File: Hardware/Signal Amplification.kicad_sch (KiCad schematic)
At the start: 0 parts

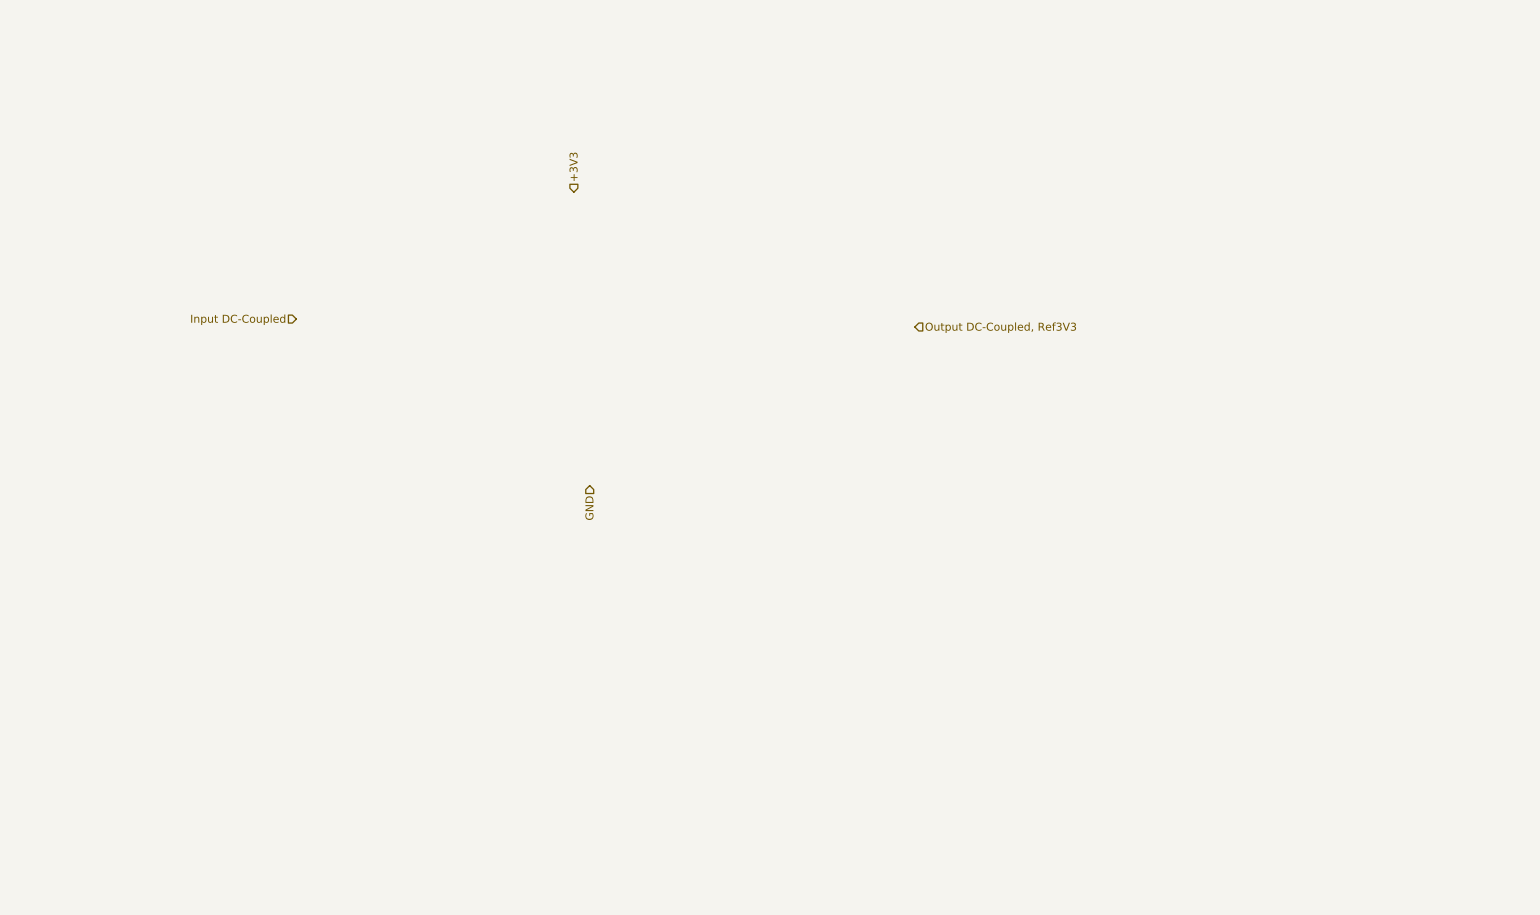
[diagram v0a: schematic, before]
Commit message: Drew the analog Signal conditioning
The analog signal conditioning can be reduced to:
- a amplification by -60
- a High-Pass filter with Fc≈20Hz -3dB
- a Low-Pass filter with Fc≈5kHz -6dB
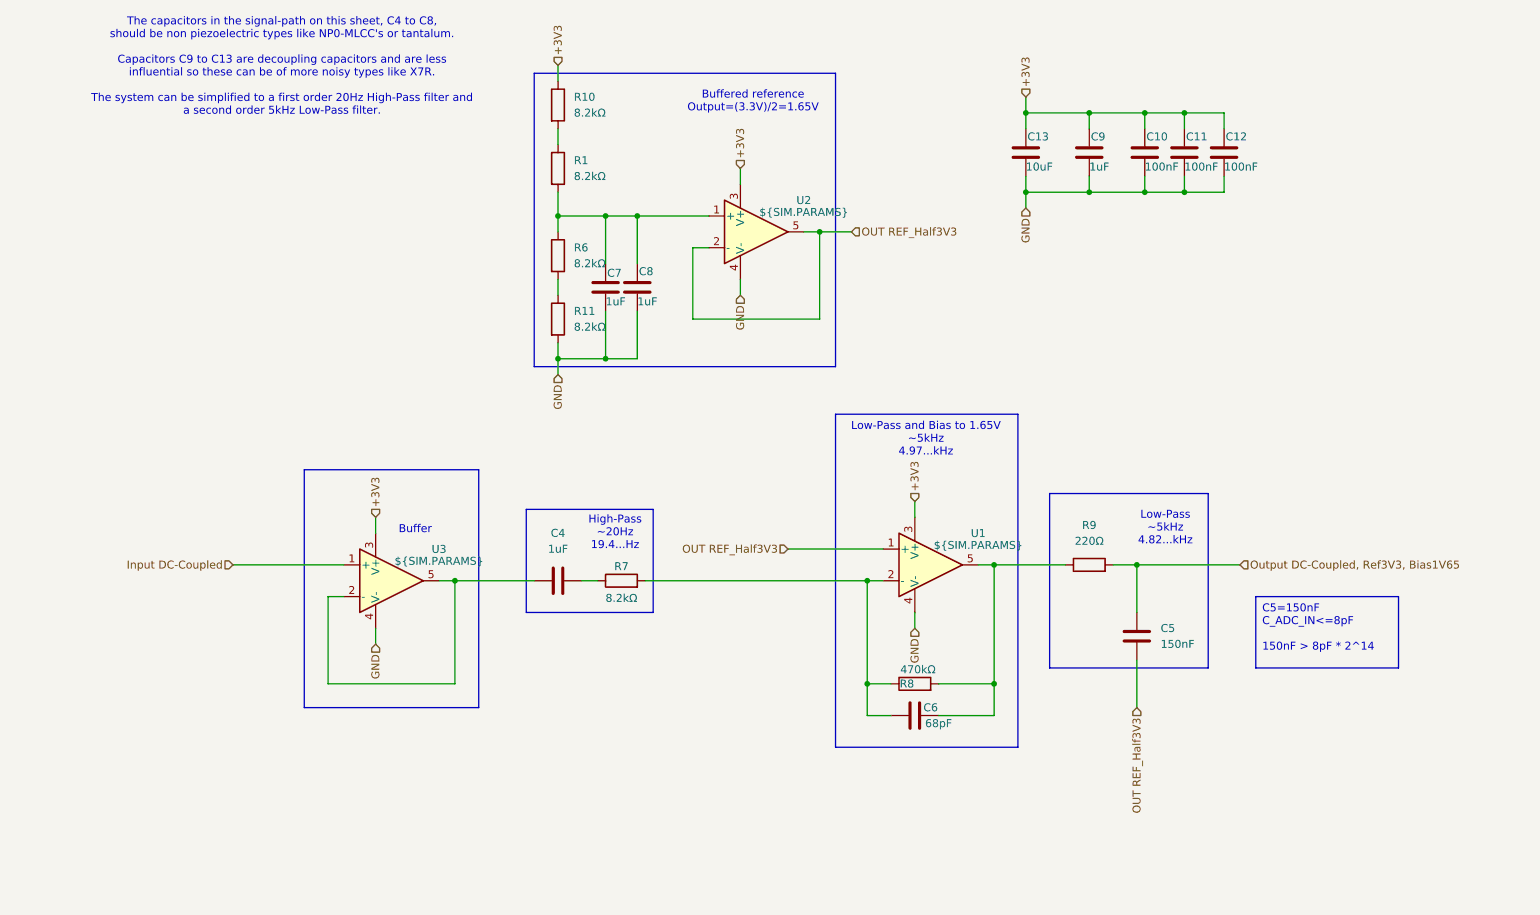
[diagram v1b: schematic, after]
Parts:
- added C10, C11, C12: 100nF, symbol Device:C
- added C13: 10uF, symbol Device:C
- added C4, C7, C8, C9: 1uF, symbol Device:C
- added C5: 150nF, symbol Device:C
- added C6: 68pF, symbol Device:C
- added R1, R10, R11, R6, R7: 8.2kΩ, symbol Device:R
- added R8: 470kΩ, symbol Device:R
- added R9: 220Ω, symbol Device:R
- added U1, U2, U3: ${SIM.PARAMS}, symbol Simulation_SPICE:OPAMP
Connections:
- net +3V3: now also C10.1, C11.1, C12.1, C13.1, C9.1, R10.1, U1.3 (V+), U2.3 (V+), U3.3 (V+)
- net GND: now also C10.2, C11.2, C12.2, C13.2, C7.2, C8.2, C9.2, R11.2, U1.4 (V-), U2.4 (V-), U3.4 (V-)
- net Input DC-Coupled: now also U3.1 (+)
- new net: C7.1, C8.1, R1.2, R6.1, U2.1 (+)
- new net: R11.1, R6.2
- new net: C6.2, R8.2, R9.1, U1.5
- new net: C4.2, R7.1
- new net: C6.1, R7.2, R8.1, U1.2 (-)
- new net: C4.1, U3.2 (-), U3.5
- new net: R1.1, R10.2
- new net OUT REF_Half3V3: C5.2, U1.1 (+), U2.2 (-), U2.5
- new net Output DC-Coupled, Ref3V3, Bias1V65: C5.1, R9.2
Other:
- note added: "Buffer"
- note added: "Buffered reference Output=(3.3V)/2=1.65V"
- note added: "High-Pass ~20Hz 19.4...Hz"
- note added: "Low-Pass and Bias to 1.65V ~5kHz 4.97...kHz"
- note added: "Low-Pass ~5kHz 4.82...kHz"
- note added: "The capacitors in the signal-path on this sheet, C4 to C8, should be non piezoelectric types like NP0-MLCC's or tantalum. Capacitors C9 to C13 are decoupling capacitors and are less influential so these can be of more noisy types like X7R. The system can be simplified to a first order 20Hz High-Pass filter and a second order 5kHz Low-Pass filter."

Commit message: split some of the text and grouped the circuits better
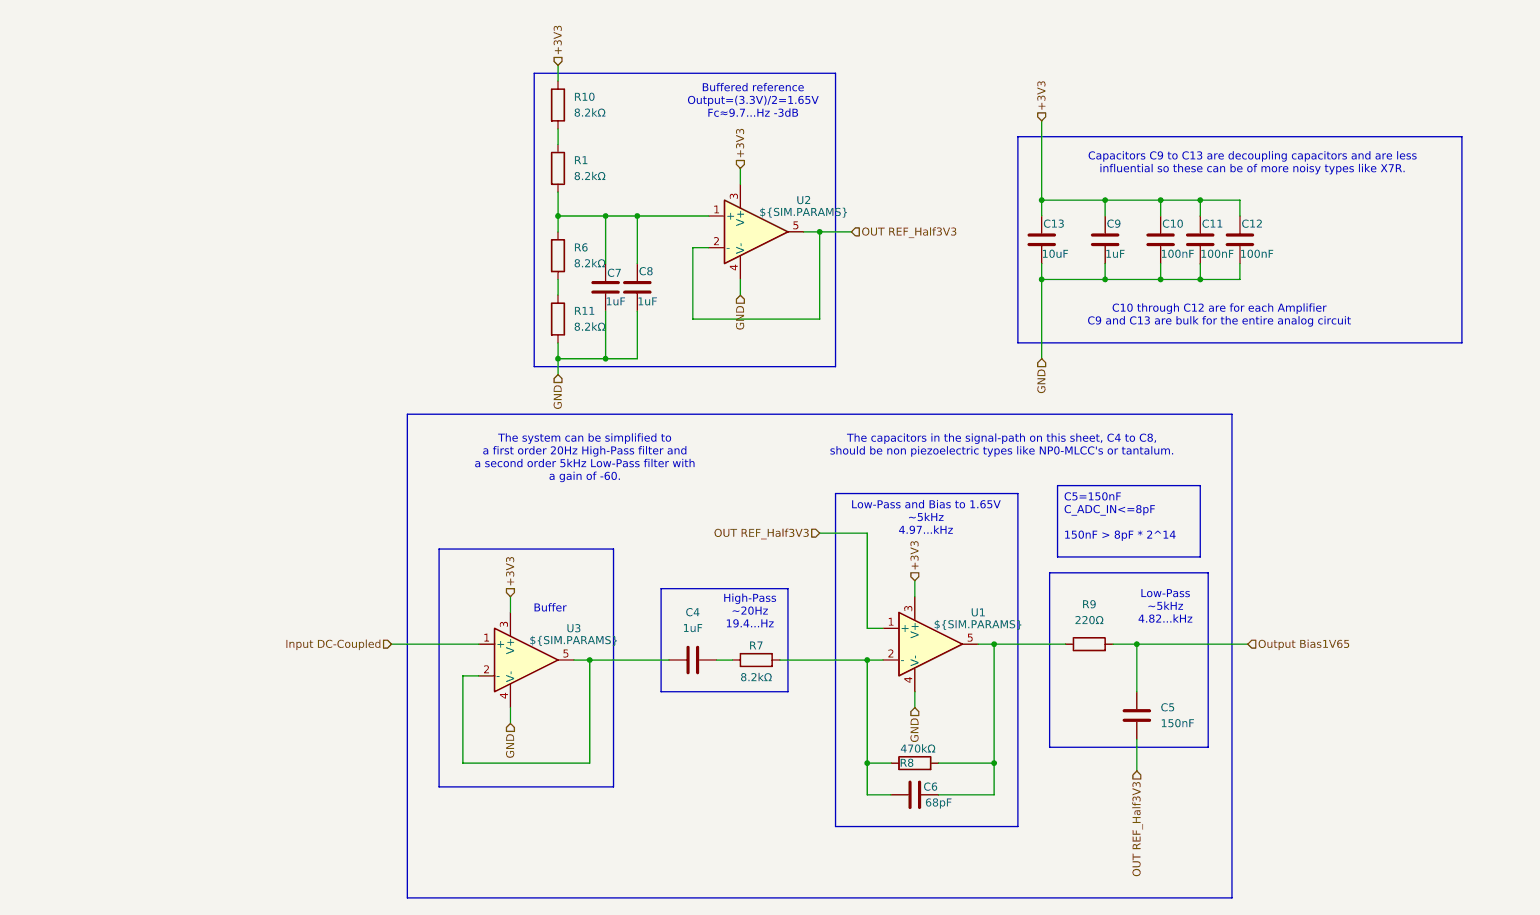
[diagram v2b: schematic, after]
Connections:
- net Output DC-Coupled, Ref3V3, Bias1V65 renamed Output Bias1V65
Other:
- note added: "Buffered reference Output=(3.3V)/2=1.65V Fc≈9.7...Hz -3dB"
- note added: "C10 through C12 are for each Amplifier C9 and C13 are bulk for the entire analog circuit"
- note added: "Capacitors C9 to C13 are decoupling capacitors and are less influential so these can be of more noisy types like X7R."
- note added: "The capacitors in the signal-path on this sheet, C4 to C8, should be non piezoelectric types like NP0-MLCC's or tantalum."
- note added: "The system can be simplified to a first order 20Hz High-Pass filter and a second order 5kHz Low-Pass filter with a gain of -60."
- note removed: "Buffered reference Output=(3.3V)/2=1.65V"
- note removed: "The capacitors in the signal-path on this sheet, C4 to C8, should be non piezoelectric types like NP0-MLCC's or tantalum. Capacitors C9 to C13 are decoupling capacitors and are less influential so these can be of more noisy types like X7R. The system can be simplified to a first order 20Hz High-Pass filter and a second order 5kHz Low-Pass filter."
- moved on the sheet: C10, C11, C12, C13, C4, C5, C6, C9, R7, R8, R9, U1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

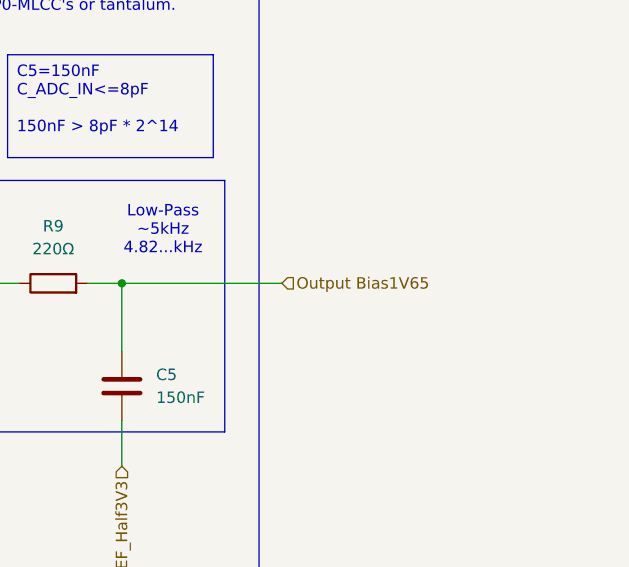
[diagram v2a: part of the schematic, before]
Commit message: changed "Output Bias1V65" to "OUT Signal Bias1V65"
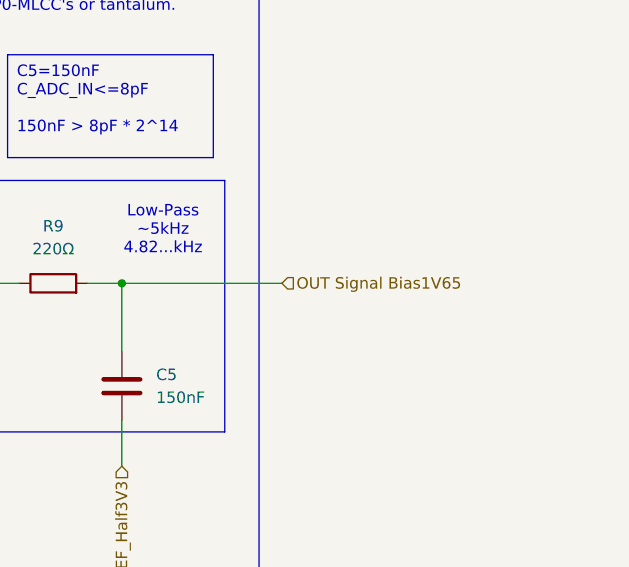
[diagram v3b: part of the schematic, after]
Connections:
- net Output Bias1V65 renamed OUT Signal Bias1V65
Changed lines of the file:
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@@
 		)
 	)
-	(hierarchical_label "Output Bias1V65"
+	(hierarchical_label "OUT Signal Bias1V65"
 		(shape input)
 		(at 203.2 115.57 0)

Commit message: Started linking footprints and work on the pcb layout
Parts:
- C10, C11, C12: footprint (none) -> Capacitor_SMD:C_0402_1005Metric_Pad0.74x0.62mm_HandSolder
- C13: footprint (none) -> Capacitor_SMD:C_0805_2012Metric_Pad1.18x1.45mm_HandSolder
- C6, C9: footprint (none) -> Capacitor_SMD:C_0603_1608Metric_Pad1.08x0.95mm_HandSolder
- R1, R10, R11, R6, R7, R8, R9: footprint (none) -> Resistor_SMD:R_0402_1005Metric_Pad0.72x0.64mm_HandSolder
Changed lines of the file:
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@@
 			)
 		)
-		(property "Footprint" ""
+		(property "Footprint" "Resistor_SMD:R_0402_1005Metric_Pad0.72x0.64mm_HandSolder"
 			(at 90.932 53.34 90)
 			(effects
@@
 			)
 		)
-		(property "Footprint" ""
+		(property "Footprint" "Resistor_SMD:R_0402_1005Metric_Pad0.72x0.64mm_HandSolder"
 			(at 177.8 117.348 90)
 			(effects
@@
 			)
 		)
-		(property "Footprint" ""
+		(property "Footprint" "Resistor_SMD:R_0402_1005Metric_Pad0.72x0.64mm_HandSolder"
 			(at 124.46 119.888 90)
 			(effects
@@
 			)
 		)
-		(property "Footprint" ""
+		(property "Footprint" "Capacitor_SMD:C_0402_1005Metric_Pad0.74x0.62mm_HandSolder"
 			(at 202.8952 54.61 0)
 			(effects
@@
 			)
 		)
-		(property "Footprint" ""
+		(property "Footprint" "Resistor_SMD:R_0402_1005Metric_Pad0.72x0.64mm_HandSolder"
 			(at 90.932 29.21 90)
 			(effects
@@
 			)
 		)
-		(property "Footprint" ""
+		(property "Footprint" "Resistor_SMD:R_0402_1005Metric_Pad0.72x0.64mm_HandSolder"
 			(at 149.86 136.398 90)
 			(effects
@@
 			)
 		)
-		(property "Footprint" ""
+		(property "Footprint" "Resistor_SMD:R_0402_1005Metric_Pad0.72x0.64mm_HandSolder"
 			(at 90.932 63.5 90)
 			(effects
@@
 			)
 		)
-		(property "Footprint" ""
+		(property "Footprint" "Capacitor_SMD:C_0402_1005Metric_Pad0.74x0.62mm_HandSolder"
 			(at 196.5452 54.61 0)
 			(effects
@@
 			)
 		)
-		(property "Footprint" ""
+		(property "Footprint" "Capacitor_SMD:C_0402_1005Metric_Pad0.74x0.62mm_HandSolder"
 			(at 190.1952 54.61 0)
 			(effects
@@
 			)
 		)
-		(property "Footprint" ""
+		(property "Footprint" "Capacitor_SMD:C_0805_2012Metric_Pad1.18x1.45mm_HandSolder"
 			(at 171.1452 54.61 0)
 			(effects
@@
 			)
 		)
-		(property "Footprint" ""
+		(property "Footprint" "Capacitor_SMD:C_0603_1608Metric_Pad1.08x0.95mm_HandSolder"
 			(at 181.3052 54.61 0)
 			(effects
@@
 			)
 		)
-		(property "Footprint" ""
+		(property "Footprint" "Capacitor_SMD:C_0603_1608Metric_Pad1.08x0.95mm_HandSolder"
 			(at 153.67 138.7348 0)
 			(effects
@@
 			)
 		)
-		(property "Footprint" ""
+		(property "Footprint" "Resistor_SMD:R_0402_1005Metric_Pad0.72x0.64mm_HandSolder"
 			(at 90.932 39.37 90)
 			(effects

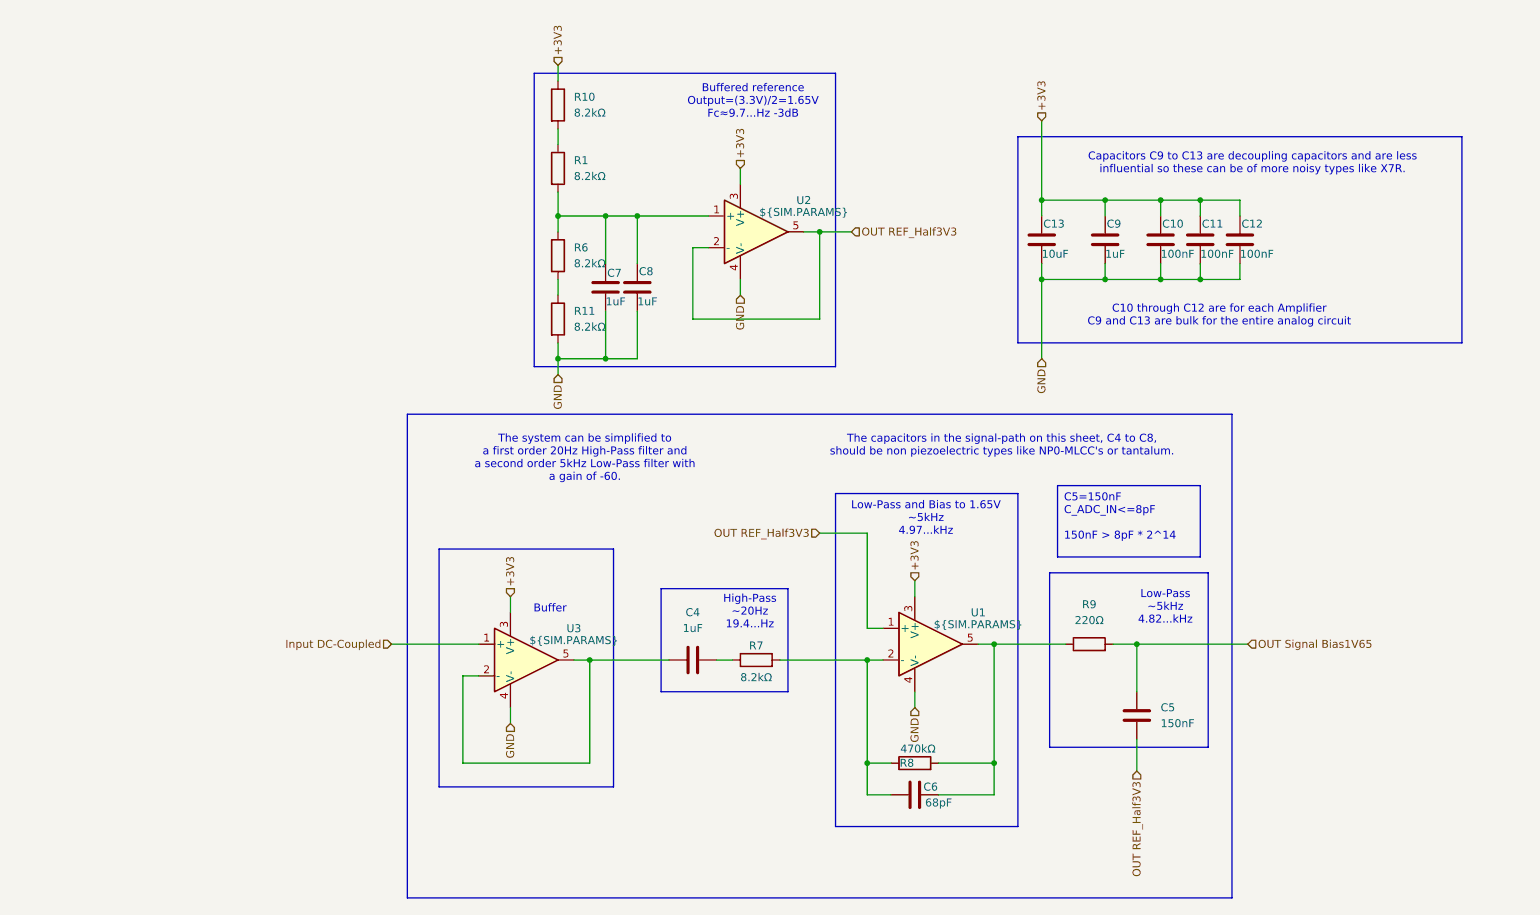
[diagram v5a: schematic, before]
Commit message: added more footprints and continued on the circuit diagram
- [ ] add antenna connection
- [ ] find suitable 390Mohm resistor
- [ ] add switches, reset and power
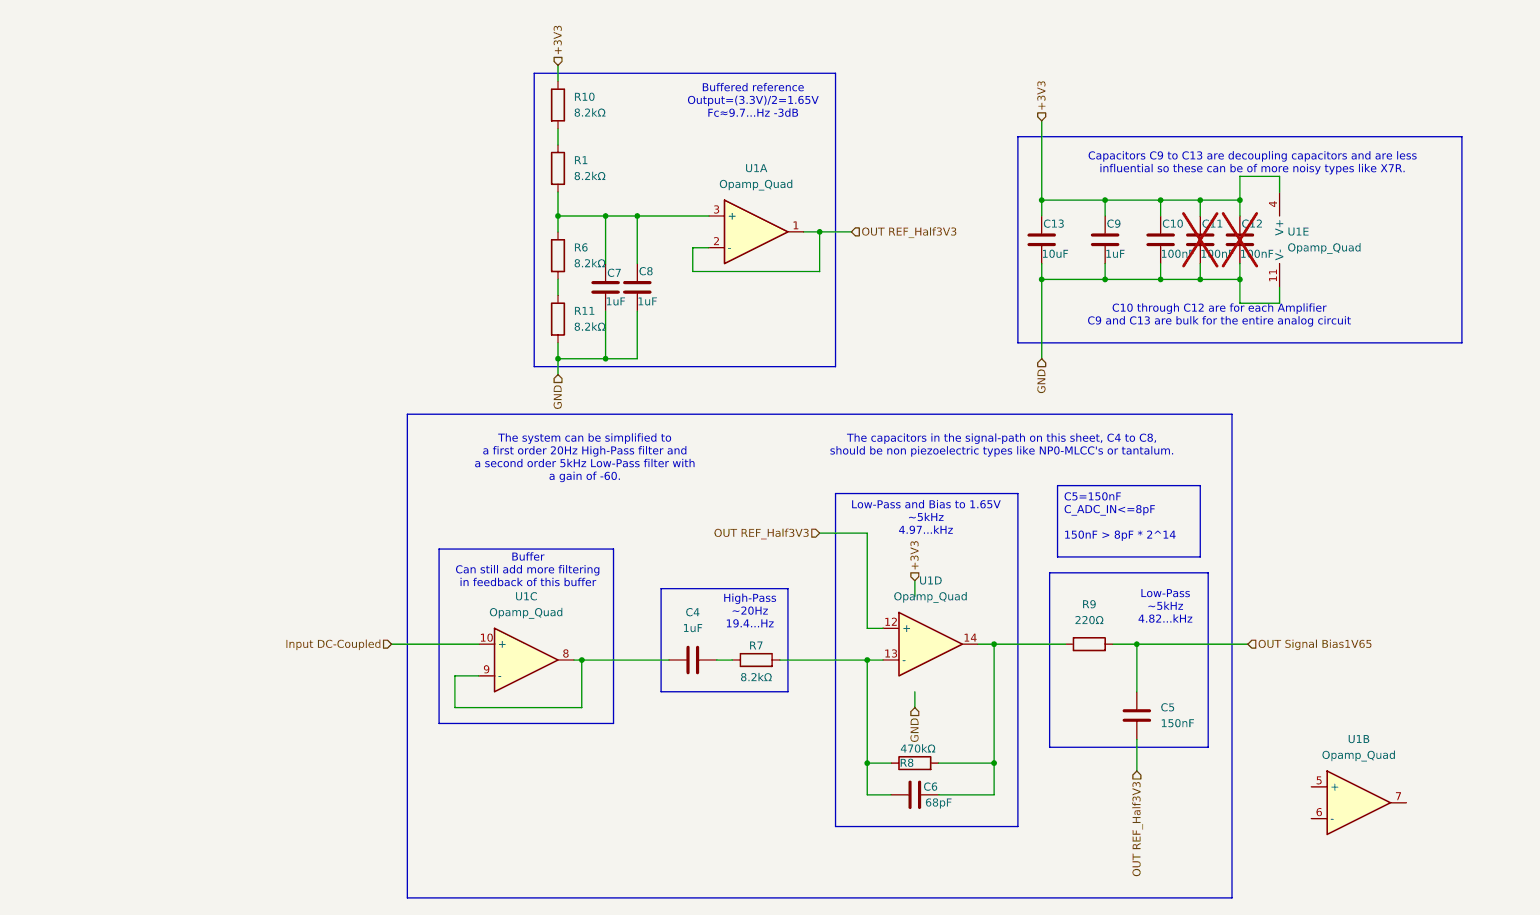
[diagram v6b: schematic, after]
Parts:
- removed U1, U2, U3: ${SIM.PARAMS}, symbol Simulation_SPICE:OPAMP
- added U1: Opamp_Quad, Package_SO:TSSOP-14_4.4x5mm_P0.65mm, symbol Device:Opamp_Quad
- C11, C12: now not fitted; now left out of the parts list
- C4, C7, C8: footprint (none) -> Capacitor_SMD:C_0805_2012Metric_Pad1.18x1.45mm_HandSolder
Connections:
- net +3V3: now also U1.4 (V+)
- net GND: now also U1.11 (V-)
- net Input DC-Coupled: now also U1.10 (+)
- net OUT REF_Half3V3: now also U1.1, U1.12 (+), U1.2 (-)
- net at C7.1, C8.1, R1.2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: now also U1.3 (+)
- net at C6.2, R8.2, R9.1: now also U1.14
- net at C6.1, R7.2, R8.1: now also U1.13 (-)
- net at C4.1: now also U1.8, U1.9 (-)
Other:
- note added: "Buffer Can still add more filtering in feedback of this buffer"
- note removed: "Buffer"
